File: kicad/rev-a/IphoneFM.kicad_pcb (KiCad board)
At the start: 2 copper layers, 46.5 x 71.4 mm, 106 parts, among them J1 USB 2.0 Type-C, J2 SMA jack, SW1 SPDT, SW2 SPST, SW3 6 × SPST, U1 MCU, U2 Synthesizer, U3 3.3 V 600 mA LDO, U4 FM receiver, U5 SPDT RF switch, U6 USB ESD array, U7 Digital step attenuator, Y2 20 MHz CMOS XO

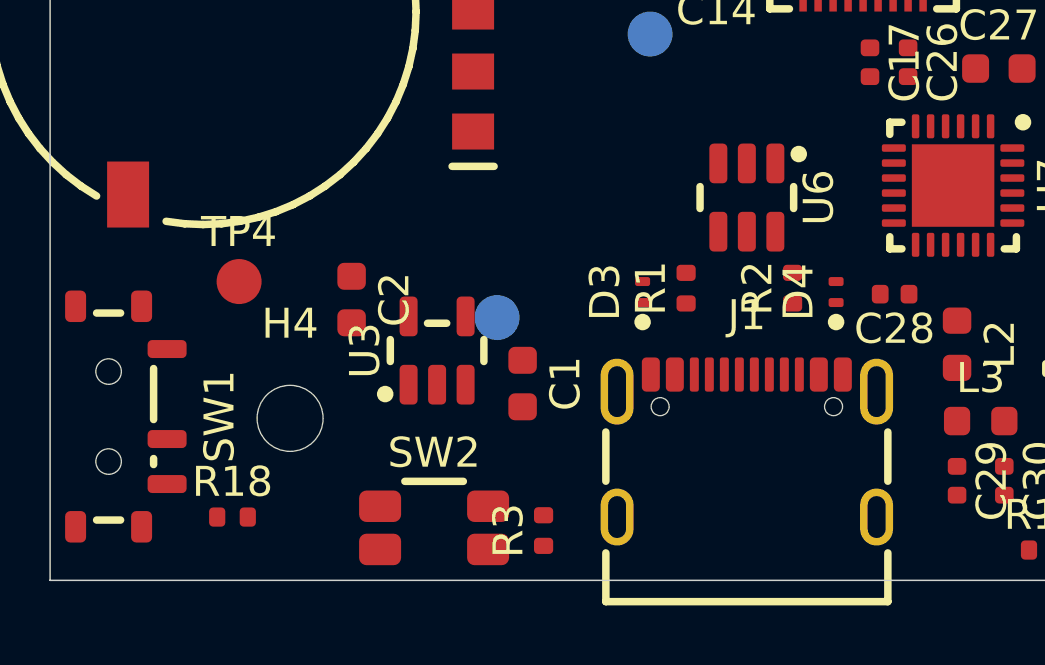
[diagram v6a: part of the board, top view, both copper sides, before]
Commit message: Phase 5 prep: J1 corner and west strip plan (pcb_route_j1.py), open-connection lister, U1/U2 gap fixes
Co-Authored-By: Claude Opus 5.5 <noreply@anthropic.com>
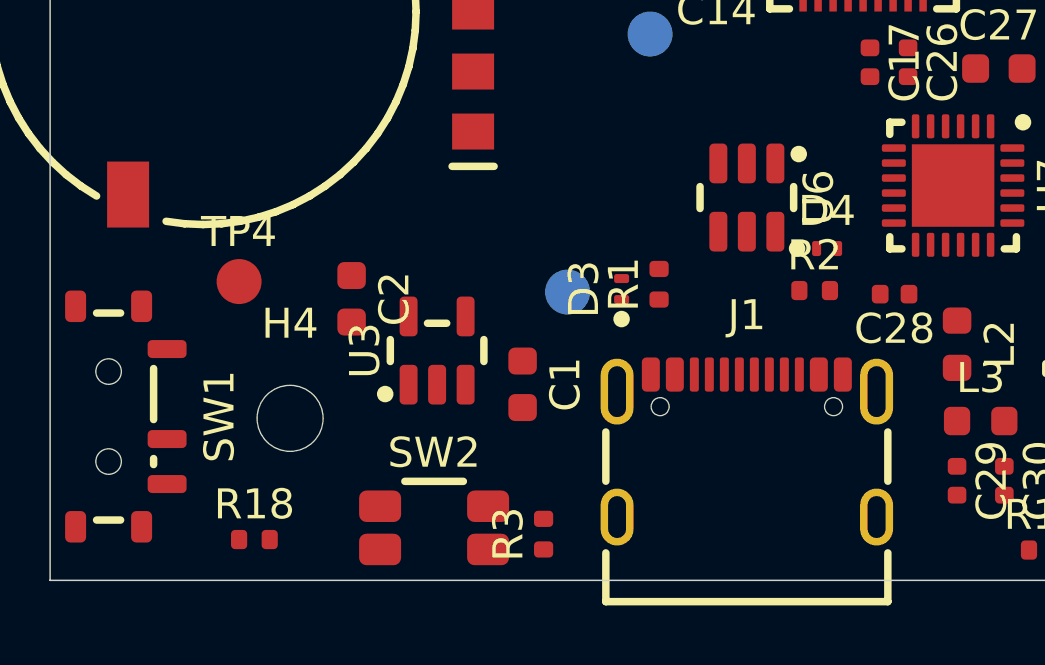
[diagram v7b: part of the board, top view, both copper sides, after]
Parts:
- moved TP1 2.50 mm to (29.9, 121.3)
- moved D4 1.48 mm to (38.6, 119.9), turned to 0 degrees
- moved R18 1.05 mm to (19.5, 129.6)
- moved R1 0.91 mm to (33.0, 121.1)
- moved R2 0.74 mm to (38.2, 121.3), turned to 0 degrees
- moved D3 0.71 mm to (31.8, 121.2)
- moved R3 0.12 mm to (29.1, 129.4)
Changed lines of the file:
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@@
 	(footprint "IphoneFM:C_0603_1608Metric"
 		(layer "F.Cu")
-		(at 22.75 121.6 -90)
+		(at 22.75 121.575 -90)
 		(descr "Capacitor SMD 0603 (1608 Metric), square (rectangular) end terminal, IPC-7351 nominal, (Body size source: IPC-SM-782 page 76, https://www.pcb-3d.com/wordpress/wp-content/uploads/ipc-sm-782a_amendment_1_and_2.pdf)")
 		(tags "capacitor")
@@
 	(footprint "IphoneFM:R_0402_1005Metric"
 		(layer "F.Cu")
-		(at 29.15 129.3 90)
+		(at 29.15 129.42 90)
 		(descr "Resistor SMD 0402 (1005 Metric), square (rectangular) end terminal, IPC-7351 nominal, (Body size source: IPC-SM-782 page 72, https://www.pcb-3d.com/wordpress/wp-content/uploads/ipc-sm-782a_amendment_1_and_2.pdf)")
 		(tags "resistor")
@@
 	(footprint "IphoneFM:R_0402_1005Metric"
 		(layer "F.Cu")
-		(at 18.78 128.85)
+		(at 19.51 129.6)
 		(descr "Resistor SMD 0402 (1005 Metric), square (rectangular) end terminal, IPC-7351 nominal, (Body size source: IPC-SM-782 page 72, https://www.pcb-3d.com/wordpress/wp-content/uploads/ipc-sm-782a_amendment_1_and_2.pdf)")
 		(tags "resistor")
@@
 		(sheetname "/")
 		(sheetfile "IphoneFM.kicad_sch")
-		(units
-			(unit
-				(name "A")
-				(pins "1" "2")
-			)
-		)
 		(attr smd)
 		(duplicate_pad_numbers_are_jumpers no)
 		(fp_rect
-			(start -0.93 -0.47)
-			(end 0.93 0.47)
+			(start -0.929999 -0.47)
+			(end 0.929999 0.47)
 			(stroke
 				(width 0.05)
@@
 		)
 		(fp_text user "${REFERENCE}"
-			(at 0 0 0)
+			(at 0 0 360)
 			(layer "F.Fab")
 			(effects
@@
 		)
 		(embedded_fonts no)
-		(model "${KICAD10_3DMODEL_DIR}/Resistor_SMD.3dshapes/R_0402_1005Metric.step"
-			(offset
-				(xyz 0 0 0)
-			)
-			(scale
-				(xyz 1 1 1)
-			)
-			(rotate
-				(xyz 0 0 0)
-			)
-		)
 	)
 	(footprint "IphoneFM:SW_SPDT_Shouhan_MSK12C02_Tabs4"
@@
 	(footprint "IphoneFM:R_0402_1005Metric"
 		(layer "F.Cu")
-		(at 33.9 121.22 90)
+		(at 33 121.09 90)
 		(descr "Resistor SMD 0402 (1005 Metric), square (rectangular) end terminal, IPC-7351 nominal, (Body size source: IPC-SM-782 page 72, https://www.pcb-3d.com/wordpress/wp-content/uploads/ipc-sm-782a_amendment_1_and_2.pdf)")
 		(tags "resistor")
@@
 		(sheetname "/")
 		(sheetfile "IphoneFM.kicad_sch")
-		(units
-			(unit
-				(name "A")
-				(pins "1" "2")
-			)
-		)
 		(attr smd)
 		(duplicate_pad_numbers_are_jumpers no)
@@
 		)
 		(embedded_fonts no)
-		(model "${KICAD10_3DMODEL_DIR}/Resistor_SMD.3dshapes/R_0402_1005Metric.step"
-			(offset
-				(xyz 0 0 0)
-			)
-			(scale
-				(xyz 1 1 1)
-			)
-			(rotate
-				(xyz 0 0 0)
-			)
-		)
 	)
 	(footprint "IphoneFM:MountingHole_2.2mm_M2"
@@
 	(footprint "IphoneFM:R_0402_1005Metric"
 		(layer "F.Cu")
-		(at 37.45 121.22 90)
+		(at 38.185 121.3)
 		(descr "Resistor SMD 0402 (1005 Metric), square (rectangular) end terminal, IPC-7351 nominal, (Body size source: IPC-SM-782 page 72, https://www.pcb-3d.com/wordpress/wp-content/uploads/ipc-sm-782a_amendment_1_and_2.pdf)")
 		(tags "resistor")
 		(property "Reference" "R2"
-			(at 0 -1.17 90)
+			(at 0 -1.17 0)
 			(layer "F.SilkS")
 			(effects
@@
 		)
 		(property "Value" "5.1 kΩ 1%"
-			(at 0 1.17 90)
+			(at 0 1.17 0)
 			(layer "F.Fab")
 			(effects
@@
 		)
 		(property "Datasheet" "~"
-			(at 0 0 90)
+			(at 0 0 0)
 			(layer "F.Fab")
 			(hide yes)
@@
 		)
 		(property "Description" ""
-			(at 0 0 90)
+			(at 0 0 0)
 			(layer "F.Fab")
 			(hide yes)
@@
 		)
 		(property "KiLib_Generator" "SMD_2terminal_chip_molded"
-			(at 0 0 90)
+			(at 0 0 0)
 			(layer "F.SilkS")
 			(hide yes)
@@
 		)
 		(property "MPN" "RC0402FR-075K1L"
-			(at 0 0 90)
+			(at 0 0 0)
 			(unlocked yes)
 			(layer "F.Fab")
@@
 		)
 		(property "LCSC" "C105872"
-			(at 0 0 90)
+			(at 0 0 0)
 			(unlocked yes)
 			(layer "F.Fab")
@@
 		)
 		(property "Manufacturer" "Yageo"
-			(at 0 0 90)
+			(at 0 0 0)
 			(unlocked yes)
 			(layer "F.Fab")
@@
 		(duplicate_pad_numbers_are_jumpers no)
 		(fp_rect
-			(start -0.93 -0.47)
-			(end 0.93 0.47)
+			(start -0.929999 -0.47)
+			(end 0.929999 0.47)
 			(stroke
 				(width 0.05)
@@
 		)
 		(fp_text user "${REFERENCE}"
-			(at 0 0 90)
+			(at 0 0 360)
 			(layer "F.Fab")
 			(effects
@@
 		)
 		(pad "1" smd roundrect
-			(at -0.51 0 90)
+			(at -0.51 0)
 			(size 0.54 0.64)
 			(layers "F.Cu" "F.Mask" "F.Paste")
@@
 		)
 		(pad "2" smd roundrect
-			(at 0.51 0 90)
+			(at 0.51 0)
 			(size 0.54 0.64)
 			(layers "F.Cu" "F.Mask" "F.Paste")
@@
 	(footprint "IphoneFM:C_0603_1608Metric"
 		(layer "F.Cu")
-		(at 28.45 124.4 -90)
+		(at 28.45 124.425 -90)
 		(descr "Capacitor SMD 0603 (1608 Metric), square (rectangular) end terminal, IPC-7351 nominal, (Body size source: IPC-SM-782 page 76, https://www.pcb-3d.com/wordpress/wp-content/uploads/ipc-sm-782a_amendment_1_and_2.pdf)")
 		(tags "capacitor")
@@
 	(footprint "IphoneFM:Texas_DPY0002A_0.6x1mm_P0.65mm"
 		(layer "F.Cu")
-		(at 38.9 121.35 90)
+		(at 38.6 119.9)
 		(descr "X1SON 2 pin 0.6x1mm 0.375mm height package, https://www.ti.com/lit/ml/mpss034c/mpss034c.pdf, https://www.ti.com/lit/ds/symlink/tpd6e05u06.pdf")
 		(tags "X1SON")
 		(property "Reference" "D4"
-			(at 0 -1.25 90)
+			(at 0 -1.25 0)
 			(unlocked yes)
 			(layer "F.SilkS")
@@
 		)
 		(property "Value" "ESD 5.5 V"
-			(at 0 1.25 90)
+			(at 0 1.25 0)
 			(unlocked yes)
 			(layer "F.Fab")
@@
 		)
 		(property "Datasheet" "~"
-			(at 0 0 90)
+			(at 0 0 0)
 			(unlocked yes)
 			(layer "F.Fab")
@@
 		)
 		(property "Description" ""
-			(at 0 0 90)
+			(at 0 0 0)
 			(unlocked yes)
 			(layer "F.Fab")
@@
 		)
 		(property "MPN" "TPD1E05U06DPYR"
-			(at 0 0 90)
+			(at 0 0 0)
 			(unlocked yes)
 			(layer "F.Fab")
@@
 		)
 		(property "LCSC" "C436349"
-			(at 0 0 90)
+			(at 0 0 0)
 			(unlocked yes)
 			(layer "F.Fab")
@@
 		)
 		(property "Manufacturer" "TI"
-			(at 0 0 90)
+			(at 0 0 0)
 			(unlocked yes)
 			(layer "F.Fab")
@@
 		)
 		(fp_rect
-			(start -0.65 -0.45)
-			(end 0.65 0.45)
+			(start -0.649999 -0.45)
+			(end 0.649999 0.45)
 			(stroke
 				(width 0.05)
@@
 		)
 		(fp_line
-			(start -0.2 0.3)
-			(end -0.2 -0.3)
+			(start -0.4 0.299999)
+			(end -0.399999 -0.3)
 			(stroke
 				(width 0.1)
@@
 		)
 		(fp_line
-			(start -0.3 0.3)
-			(end -0.3 -0.3)
+			(start -0.3 0.299999)
+			(end -0.299999 -0.3)
 			(stroke
 				(width 0.1)
@@
 		)
 		(fp_line
-			(start -0.4 0.3)
-			(end -0.4 -0.3)
+			(start -0.2 0.299999)
+			(end -0.199999 -0.3)
 			(stroke
 				(width 0.1)
@@
 		)
 		(fp_rect
-			(start -0.5 -0.3)
-			(end 0.5 0.3)
+			(start -0.499999 -0.3)
+			(end 0.499999 0.3)
 			(stroke
 				(width 0.1)
@@
 		)
 		(fp_text user "${REFERENCE}"
-			(at 0 0 90)
+			(at 0 0 360)
 			(layer "F.Fab")
 			(effects
@@
 		)
 		(pad "1" smd roundrect
-			(at -0.35 0 90)
+			(at -0.35 0)
 			(size 0.3 0.5)
 			(layers "F.Cu" "F.Mask" "F.Paste")
@@
 		)
 		(pad "2" smd roundrect
-			(at 0.35 0 90)
+			(at 0.35 0)
 			(size 0.3 0.5)
 			(layers "F.Cu" "F.Mask" "F.Paste")
@@
 	(footprint "IphoneFM:Texas_DPY0002A_0.6x1mm_P0.65mm"
 		(layer "F.Cu")
-		(at 32.45 121.35 90)
+		(at 31.75 121.25 90)
 		(descr "X1SON 2 pin 0.6x1mm 0.375mm height package, https://www.ti.com/lit/ml/mpss034c/mpss034c.pdf, https://www.ti.com/lit/ds/symlink/tpd6e05u06.pdf")
 		(tags "X1SON")
@@
 		(sheetname "/")
 		(sheetfile "IphoneFM.kicad_sch")
-		(units
-			(unit
-				(name "A")
-				(pins "1" "2")
-			)
-		)
 		(attr smd)
 		(duplicate_pad_numbers_are_jumpers no)
@@
 		)
 		(embedded_fonts no)
-		(model "${KICAD10_3DMODEL_DIR}/Package_SON.3dshapes/Texas_DPY0002A_0.6x1mm_P0.65mm.step"
-			(offset
-				(xyz 0 0 0)
-			)
-			(scale
-				(xyz 1 1 1)
-			)
-			(rotate
-				(xyz 0 0 0)
-			)
-		)
 	)
 	(footprint "IphoneFM:R_0402_1005Metric"
@@
 	(footprint "IphoneFM:TestPoint_Pad_D1.5mm"
 		(layer "B.Cu")
-		(at 27.6 122.2 180)
+		(at 29.95 121.35 180)
 		(descr "SMD pad as test Point, diameter 1.5mm")
 		(tags "test point SMD pad")

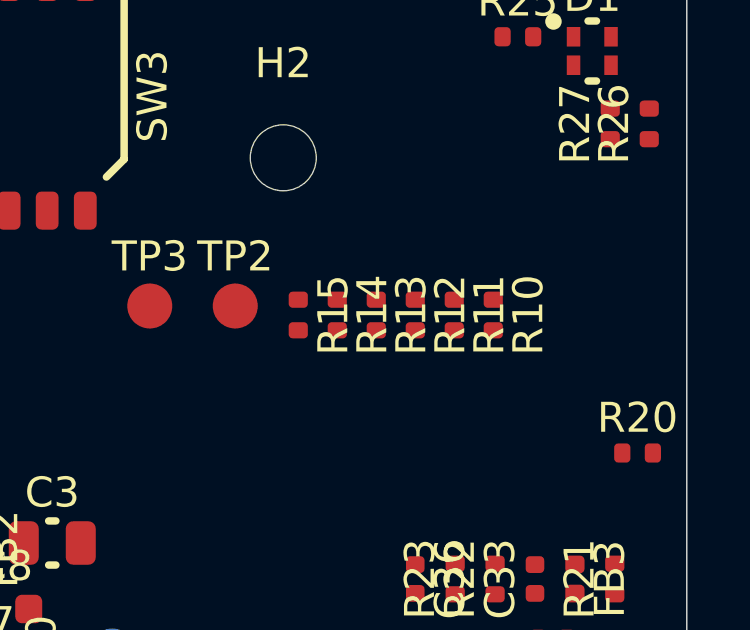
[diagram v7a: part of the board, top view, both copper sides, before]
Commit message: Phase 5 WIP: RST moved to the top layer beside the receiver bundle; attenuator bus plan started (pcb_route_att.py), R10-R15 1.7 mm east
Co-Authored-By: Claude Opus 5.5 <noreply@anthropic.com>
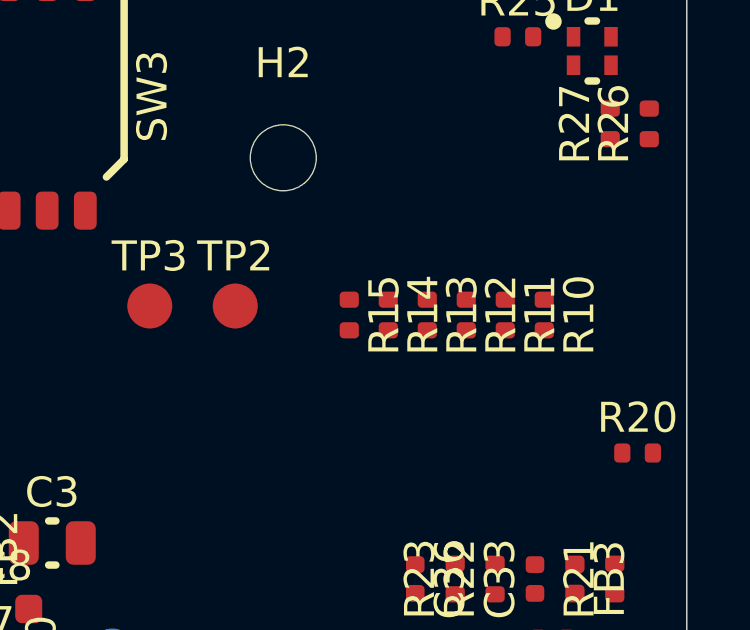
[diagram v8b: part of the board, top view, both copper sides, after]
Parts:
- moved R11 1.70 mm to (53.1, 71.8)
- moved R13 1.70 mm to (50.5, 71.8)
- moved R14 1.70 mm to (49.2, 71.8)
- moved R10 1.70 mm to (54.4, 71.8)
- moved R12 1.70 mm to (51.8, 71.8)
- moved R15 1.70 mm to (47.9, 71.8)
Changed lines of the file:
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@@
 	(footprint "IphoneFM:R_0402_1005Metric"
 		(layer "F.Cu")
-		(at 52.7 71.8 -90)
+		(at 54.4 71.8 -90)
 		(descr "Resistor SMD 0402 (1005 Metric), square (rectangular) end terminal, IPC-7351 nominal, (Body size source: IPC-SM-782 page 72, https://www.pcb-3d.com/wordpress/wp-content/uploads/ipc-sm-782a_amendment_1_and_2.pdf)")
 		(tags "resistor")
@@
 	(footprint "IphoneFM:R_0402_1005Metric"
 		(layer "F.Cu")
-		(at 46.2 71.8 -90)
+		(at 47.9 71.8 -90)
 		(descr "Resistor SMD 0402 (1005 Metric), square (rectangular) end terminal, IPC-7351 nominal, (Body size source: IPC-SM-782 page 72, https://www.pcb-3d.com/wordpress/wp-content/uploads/ipc-sm-782a_amendment_1_and_2.pdf)")
 		(tags "resistor")
@@
 	(footprint "IphoneFM:R_0402_1005Metric"
 		(layer "F.Cu")
-		(at 50.1 71.8 -90)
+		(at 51.8 71.8 -90)
 		(descr "Resistor SMD 0402 (1005 Metric), square (rectangular) end terminal, IPC-7351 nominal, (Body size source: IPC-SM-782 page 72, https://www.pcb-3d.com/wordpress/wp-content/uploads/ipc-sm-782a_amendment_1_and_2.pdf)")
 		(tags "resistor")
@@
 	(footprint "IphoneFM:R_0402_1005Metric"
 		(layer "F.Cu")
-		(at 48.8 71.8 -90)
+		(at 50.5 71.8 -90)
 		(descr "Resistor SMD 0402 (1005 Metric), square (rectangular) end terminal, IPC-7351 nominal, (Body size source: IPC-SM-782 page 72, https://www.pcb-3d.com/wordpress/wp-content/uploads/ipc-sm-782a_amendment_1_and_2.pdf)")
 		(tags "resistor")
@@
 	(footprint "IphoneFM:R_0402_1005Metric"
 		(layer "F.Cu")
-		(at 51.4 71.8 -90)
+		(at 53.1 71.8 -90)
 		(descr "Resistor SMD 0402 (1005 Metric), square (rectangular) end terminal, IPC-7351 nominal, (Body size source: IPC-SM-782 page 72, https://www.pcb-3d.com/wordpress/wp-content/uploads/ipc-sm-782a_amendment_1_and_2.pdf)")
 		(tags "resistor")
@@
 	(footprint "IphoneFM:R_0402_1005Metric"
 		(layer "F.Cu")
-		(at 47.5 71.8 -90)
+		(at 49.2 71.8 -90)
 		(descr "Resistor SMD 0402 (1005 Metric), square (rectangular) end terminal, IPC-7351 nominal, (Body size source: IPC-SM-782 page 72, https://www.pcb-3d.com/wordpress/wp-content/uploads/ipc-sm-782a_amendment_1_and_2.pdf)")
 		(tags "resistor")
